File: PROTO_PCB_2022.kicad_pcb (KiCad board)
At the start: 2 copper layers, 0 parts

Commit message: Updated ECU connector
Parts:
- added BRAKELIGHTS_EN1: Conn_?, Footprint Library:Molex_Proto_Microfit_Footprint, F.Cu at (193.0, 104.1)
- added BRAKELIGHTS_MOSFET1: Q3, Package_TO_SOT_SMD:SOT-23, F.Cu at (164.8, 123.2)
- added HORN_EN1: Conn_?, Footprint Library:Molex_Proto_Microfit_Footprint, F.Cu at (193.0, 129.5)
- added HORN_MOSFET1: Q1, Package_TO_SOT_SMD:SOT-23, F.Cu at (165.1, 130.8)
- added J1: ECU_EN_CONNECTION, Connector_Molex:Molex_CLIK-Mate_502386-0470_1x04-1MP_P1.25mm_Horizontal, F.Cu at (115.6, 96.5)
- added J2: SMALL_12V_BATTERY_CONNECTOR, TerminalBlock_Phoenix:TerminalBlock_Phoenix_PT-1,5-2-5.0-H_1x02_P5.00mm_Horizontal, F.Cu at (113.0, 124.5)
- added J3: 12V_EXTRA, TerminalBlock_Phoenix:TerminalBlock_Phoenix_PT-1,5-2-5.0-H_1x02_P5.00mm_Horizontal, F.Cu at (113.0, 152.4)
- added K1: RT214012, Relay_THT:Relay_SPDT_Schrack-RT1-FormC_RM5mm, F.Cu at (141.0, 108.0)
- added K2: RT214012, Relay_THT:Relay_SPDT_Schrack-RT1-FormC_RM5mm, F.Cu at (141.0, 156.2)
- added R1: 10k, Resistor_SMD:R_0805_2012Metric, F.Cu at (153.7, 129.5)
- added R2: 10k, Resistor_SMD:R_0805_2012Metric, F.Cu at (153.7, 121.9)
- added STARTER_MOTOR_EN1: Conn_?, Footprint Library:Molex_Proto_Microfit_Footprint, F.Cu at (193.0, 154.9)

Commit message: added new TVS diodes to schematic
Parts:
- added D1: HORN_D_TVS, Diode_SMD:D_SMB, F.Cu at (214.6, 92.7)
- added D2: BRAKELIGHTS_D_TVS, Diode_SMD:D_SMB, F.Cu at (209.6, 82.5)
- added J1: ECU_EN_CONNECTON_1, Connector_Molex:Molex_Micro-Fit_3.0_43650-0215_1x02_P3.00mm_Vertical, F.Cu at (166.3, 65.3)
- added J4: ECU_EN_CONECTION_2, Connector_Molex:Molex_Micro-Fit_3.0_43650-0215_1x02_P3.00mm_Vertical, F.Cu at (196.8, 71.1)
- added J5: ECU_EN_CONECTION_3, Connector_Molex:Molex_Micro-Fit_3.0_43650-0215_1x02_P3.00mm_Vertical, F.Cu at (178.0, 65.3)
- Q1: renamed from HORN_MOSFET1; value Q1 -> HORN_MOSFET1
- Q2: renamed from BRAKELIGHTS_MOSFET1; value Q3 -> BRAKELIGHTS_MOSFET1
- moved J3 41.3 mm to (85.1, 121.9)
- moved J2 41.3 mm to (85.1, 94.0)
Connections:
- J2 pad 2: SMALL_12V -> ECU_KILL_EN_TOGGLESWITCH_1A
- J3 pad 2: SMALL_12V -> ECU_KILL_EN_TOGGLESWITCH_1A
- K2 pad 14: SMALL_12V -> ECU_KILL_EN_TOGGLESWITCH_1A
- Q1 pad 1: SMALL_12V -> ECU_KILL_EN_TOGGLESWITCH_1A
- Q2 pad 1: SMALL_12V -> ECU_KILL_EN_TOGGLESWITCH_1A

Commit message: board layout done
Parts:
- removed the J1 at (115.6, 96.5)
- removed K1: RT214012, Relay_THT:Relay_SPDT_Schrack-RT1-FormC_RM5mm
- moved STARTER_MOTOR_EN1 118.1 mm to (97.8, 85.1), turned to 90 degrees
- moved J3 86.9 mm to (163.8, 85.1), turned to 180 degrees
- moved D1 82.9 mm to (134.6, 114.3)
- moved J4 77.3 mm to (120.7, 83.8)
- moved K2 76.8 mm to (92.7, 96.5), turned to 270 degrees
- moved D2 76.5 mm to (134.6, 97.8)
- moved J5 72.4 mm to (108.0, 83.8)
- moved J2 66.6 mm to (151.1, 85.1), turned to 180 degrees
- moved Q2 37.9 mm to (132.1, 104.1), turned to 270 degrees
- moved J1 37.8 mm to (133.3, 83.8)
- moved Q1 34.2 mm to (132.1, 121.9), turned to 270 degrees
- moved HORN_EN1 29.9 mm to (163.8, 123.2)
- moved BRAKELIGHTS_EN1 29.2 mm to (163.8, 105.4)
- moved R2 24.3 mm to (137.2, 104.1), turned to 270 degrees
- moved R1 18.2 mm to (137.2, 121.9), turned to 270 degrees

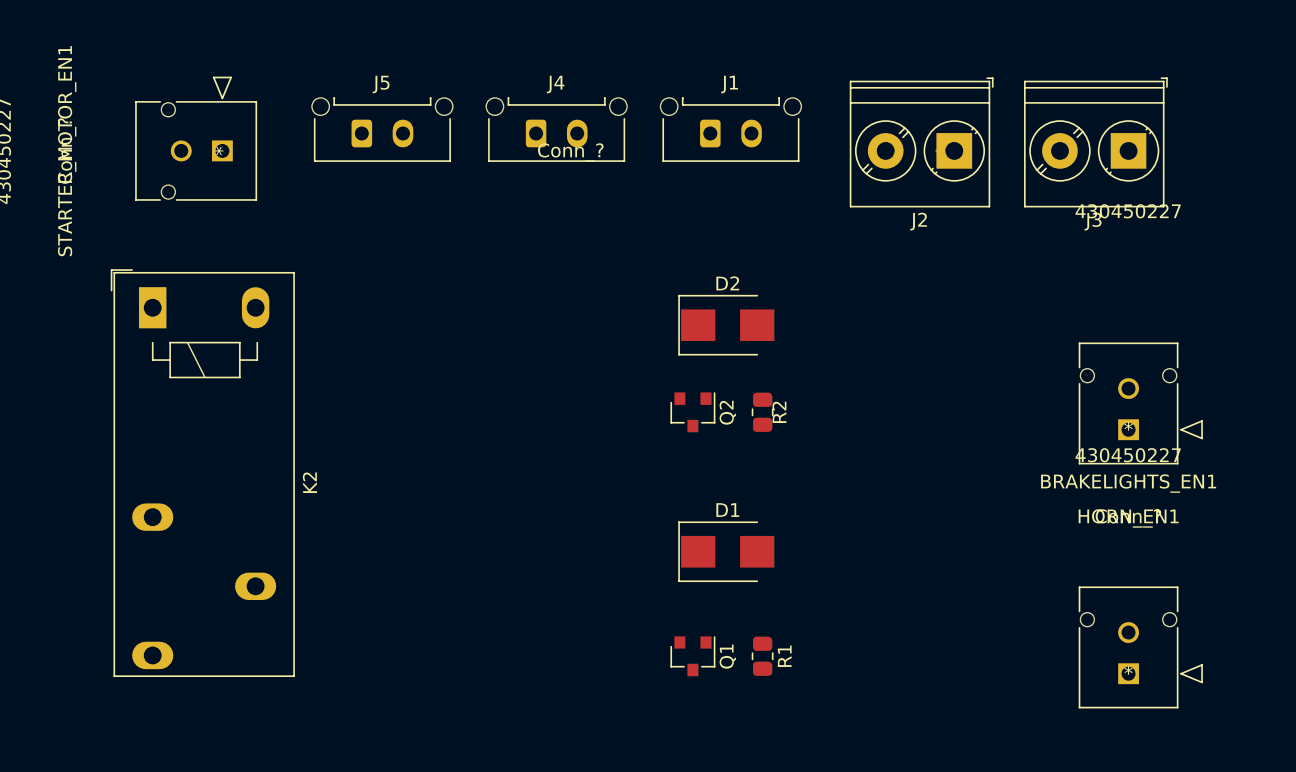
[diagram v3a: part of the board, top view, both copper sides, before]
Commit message: layout completed: components arranged, traces created
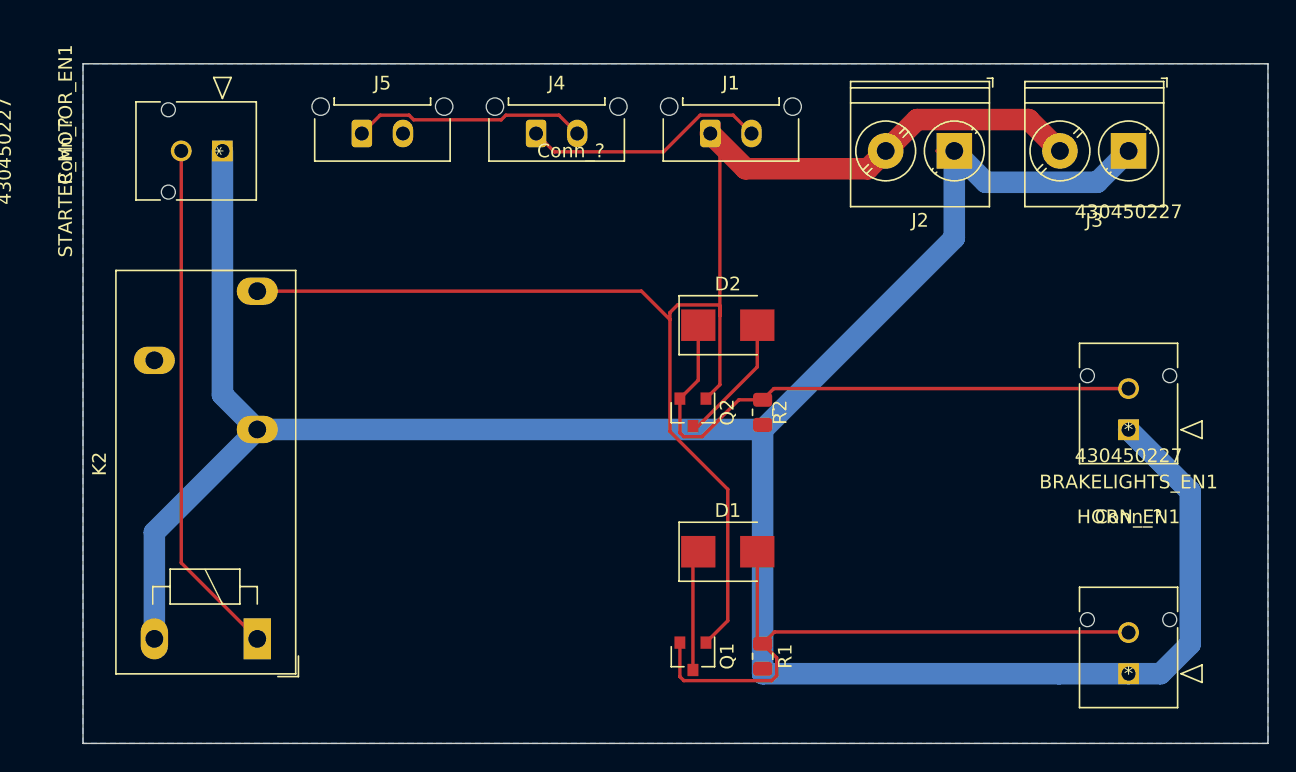
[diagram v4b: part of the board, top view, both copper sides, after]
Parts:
- moved K2 25.3 mm to (100.3, 120.7), turned to 90 degrees
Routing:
- net GND: track 0.08 -> 184.7 mm
- net ECU_KILL_EN_TOGGLESWITCH_1A: track 0.00 -> 111.0 mm
- net HORN_EN_12V_SIGNAL: track 0.00 -> 46.5 mm
- net BRAKELIGHTS_EN_12V_SIGNAL: track 0.00 -> 42.7 mm
- net STARTER_EN_PUSHBUTTON: track 0.00 -> 37.9 mm
- net ECU_KILL_EN_TOGGLESWITCH_1B: track 0.00 -> 17.9 mm
- net ECU_KILL_EN_TOGGLESWITCH_2B: track 0.00 -> 17.1 mm
- net BRAKELIGHTS_PWR: track 0.00 -> 9.52 mm
- net HORN_PWR: track 0.00 -> 8.78 mm
- added copper zone on B.Cu, net GND
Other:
- board outline added: 86.4 x 49.5 mm

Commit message: Draft PCB for Report Purposes
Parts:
- removed the J1 at (133.3, 83.8)
- removed the J4 at (120.7, 83.8)
- removed the J5 at (108.0, 83.8)
- added J10: VESC_EN_SIGNAL, Footprint Library:Molex_Proto_Microfit_Footprint, F.Cu at (112.4, 84.5)
- added J11: BRAKELIGHTS_PWR_OUT, Footprint Library:Molex_Proto_Microfit_Footprint, F.Cu at (80.2, 84.5)
- added J12: HORN_PWR_OUT, Footprint Library:Molex_Proto_Microfit_Footprint, F.Cu at (96.5, 84.5)
- added J6: ECU_POWER_DIST, TerminalBlock_Phoenix:TerminalBlock_Phoenix_PT-1,5-2-5.0-H_1x02_P5.00mm_Horizontal, F.Cu at (156.8, 111.8)
- added J7: ECU_KILL_1, Footprint Library:Molex_Proto_Microfit_Footprint, F.Cu at (128.3, 84.5)
- added J8: ECU_KILL_2, Footprint Library:Molex_Proto_Microfit_Footprint, F.Cu at (144.7, 84.5)
- added J9: ECU_KILL_3, Footprint Library:Molex_Proto_Microfit_Footprint, F.Cu at (161.1, 84.5)
- D1: renamed from D2; value BRAKELIGHTS_D_TVS -> (none)
- D2: renamed from D1; value HORN_D_TVS -> (none)
- J1: renamed from HORN_EN1; value Conn_? -> HORN_EN1
- J2: renamed from BRAKELIGHTS_EN1; value Conn_? -> BRAKELIGHTS_EN1
- J3: renamed from STARTER_MOTOR_EN1; value Conn_? -> STARTER_MOTOR_EN
- J4: renamed from J2; value SMALL_12V_BATTERY_CONNECTOR -> 12V_BATT1
- K1: renamed from K2; value RT214012 -> (none)
- Q1: renamed from Q2; value BRAKELIGHTS_MOSFET1 -> (none)
- Q2: renamed from Q1; value HORN_MOSFET1 -> (none)
- R1: renamed from R2; value 10k -> (none)
- R2: renamed from R1; value 10k -> (none)
- moved J2 87.7 mm to (76.4, 112.4), turned to 270 degrees
- moved J1 71.9 mm to (92.8, 112.4), turned to 270 degrees
- moved D1 59.1 mm to (75.6, 98.8), turned to 90 degrees
- moved R1 55.7 mm to (81.6, 101.6), turned to 0 degrees
- moved K1 54.3 mm to (148.0, 94.6), turned to 180 degrees
- moved Q1 51.0 mm to (81.5, 96.9), turned to 0 degrees
- moved D2 45.3 mm to (92.1, 98.7), turned to 270 degrees
- moved R2 44.1 mm to (98.1, 101.5), turned to 0 degrees
- moved Q2 42.3 mm to (98.1, 96.9), turned to 0 degrees
- moved J4 37.7 mm to (124.5, 111.8), turned to 0 degrees
- moved J5 35.3 mm to (140.7, 111.8), turned to 0 degrees
- moved J3 29.4 mm to (108.6, 112.4), turned to 270 degrees
- renumbered J3 to J5
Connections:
- D1 pad 2: BRAKELIGHTS_PWR -> GND
- D2 pad 1: HORN_PWR -> GND
- K1 pad 11: VESC_POWER_CONNECTION -> VESC_EN_SIGNAL
- Q1 pad 1: ECU_KILL_EN_TOGGLESWITCH_1A -> BRAKELIGHTS_PWR_OUT
- Q1 pad 3: BRAKELIGHTS_PWR -> GND
- Q2 pad 1: ECU_KILL_EN_TOGGLESWITCH_1A -> HORN_PWR_OUT
- Q2 pad 3: HORN_PWR -> GND
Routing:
- net GND: track 184.7 -> 26.5 mm, vias 0 -> 10
- net ECU_KILL_EN_TOGGLESWITCH_1A: track 111.0 -> 60.9 mm
- net ECU_KILL_EN_TOGGLESWITCH_3B: track 0.00 -> 27.6 mm
- net VESC_EN_SIGNAL: track 0.00 -> 26.2 mm
- net STARTER_EN_PUSHBUTTON: track 37.9 -> 63.4 mm
- net HORN_EN_12V_SIGNAL: track 46.5 -> 23.4 mm
- net BRAKELIGHTS_EN_12V_SIGNAL: track 42.7 -> 19.8 mm
- net HORN_PWR_OUT: track 0.00 -> 12.9 mm
- net BRAKELIGHTS_PWR_OUT: track 0.00 -> 12.9 mm
- net BRAKELIGHTS_PWR: track 9.52 -> 0.00 mm
- net HORN_PWR: track 8.78 -> 0.00 mm
- net ECU_KILL_EN_TOGGLESWITCH_1B: track 17.9 -> 13.5 mm
- net ECU_KILL_EN_TOGGLESWITCH_2B: track 17.1 -> 13.4 mm
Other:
- board size 86.4 x 49.5 mm -> 94 x 39.4 mm
- board text added: "UBC Supermileage Proto SAE 2022"

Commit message: second version
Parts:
- removed the J11 at (80.2, 84.5)
- removed the J12 at (96.5, 84.5)
- removed K1: , Relay_THT:Relay_SPDT_Schrack-RT1-FormC_RM5mm
- added H1: MountingHole, MountingHole:MountingHole_2.7mm_M2.5, F.Cu at (155.6, 98.4)
- added H2: MountingHole, MountingHole:MountingHole_2.7mm_M2.5, F.Cu at (77.5, 98.4)
- added J3: BRAKELIGHTS_CONN, TerminalBlock_Phoenix:TerminalBlock_Phoenix_PT-1,5-2-5.0-H_1x02_P5.00mm_Horizontal, F.Cu at (80.6, 85.1)
- added J6: HORN_CONN, TerminalBlock_Phoenix:TerminalBlock_Phoenix_PT-1,5-2-5.0-H_1x02_P5.00mm_Horizontal, F.Cu at (92.7, 85.1)
- added R3: , Resistor_SMD:R_0603_1608Metric, F.Cu at (110.2, 91.9)
- added U1: , Package_TO_SOT_SMD:SOT-223-3_TabPin2, F.Cu at (120.4, 98.6)
- R1: renamed from R2; value (none) -> 10k
- moved D1 12.8 mm to (104.9, 98.9)
- moved D2 11.4 mm to (87.0, 98.8)
- moved Q2 11.4 mm to (93.0, 96.9)
- moved R2 11.4 mm to (93.0, 101.6)
- moved J10 4.45 mm to (140.3, 84.5)
- moved J11 4.45 mm to (156.7, 84.5)
- moved J9 4.45 mm to (123.8, 84.5)
- moved J5 4.44 mm to (108.0, 84.5)
- moved J8 4.44 mm to (152.4, 111.8)
- moved J7 3.17 mm to (127.7, 111.8)
- moved J1 2.54 mm to (95.3, 112.4)
- moved J2 2.54 mm to (79.0, 112.4)
- moved J4 2.54 mm to (111.1, 112.4)
- moved R1 0.65 mm to (98.7, 101.6)
- moved Q1 0.64 mm to (98.7, 96.9)
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- renumbered D2 to D1, D1 to D2, J8 to J10, J9 to J11, J5 to J12, J3 to J4, J10 to J5, J4 to J7, J6 to J8, J7 to J9, Q2 to Q1, Q1 to Q2, R1 to R2
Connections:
- net ECU_KILL_EN_TOGGLESWITCH_1A renamed 12V_FOR_BRAKELIGHTS
- D1 pad 2: HORN_EN_12V_SIGNAL -> HORN_EN_5V
- D2 pad 1: BRAKELIGHTS_EN_12V_SIGNAL -> BRAKELIGHTS_EN_5V
- J1 pad 1: GND -> HORN_EN_5V
- J1 pad 2: HORN_EN_12V_SIGNAL -> +5V
- J2 pad 1: GND -> BRAKELIGHTS_EN_5V
- J2 pad 2: BRAKELIGHTS_EN_12V_SIGNAL -> +5V
- J4 pad 1: GND -> VESC_EN_5V
- J4 pad 2: STARTER_EN_PUSHBUTTON -> +5V
- J5 pad 1: GND -> Net-(J5-Pad1)
- J5 pad 2: VESC_EN_SIGNAL -> VESC_EN_5V
- Q1 pad 1: HORN_PWR_OUT -> HORN_GND
- Q1 pad 2: HORN_EN_12V_SIGNAL -> HORN_EN_5V
- Q2 pad 1: BRAKELIGHTS_PWR_OUT -> BRAKELIGHTS_GND
- Q2 pad 2: BRAKELIGHTS_EN_12V_SIGNAL -> BRAKELIGHTS_EN_5V
- R1 pad 1: HORN_EN_12V_SIGNAL -> HORN_EN_5V
- R2 pad 1: BRAKELIGHTS_EN_12V_SIGNAL -> BRAKELIGHTS_EN_5V
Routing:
- net STARTER_EN_PUSHBUTTON: track 63.4 -> 0.00 mm
- net +5V: track 0.00 -> 61.1 mm
- net 12V_FOR_BRAKELIGHTS: track 60.9 -> 98.3 mm
- net VESC_EN_5V: track 0.00 -> 30.5 mm
- net VESC_EN_SIGNAL: track 26.2 -> 0.00 mm
- net HORN_EN_5V: track 0.00 -> 24.8 mm
- net BRAKELIGHTS_EN_5V: track 0.00 -> 24.6 mm
- net HORN_EN_12V_SIGNAL: track 23.4 -> 0.00 mm
- net BRAKELIGHTS_EN_12V_SIGNAL: track 19.8 -> 0.00 mm
- net BRAKELIGHTS_GND: track 0.00 -> 15.8 mm
- net HORN_GND: track 0.00 -> 12.9 mm
- net HORN_PWR_OUT: track 12.9 -> 0.00 mm
- net BRAKELIGHTS_PWR_OUT: track 12.9 -> 0.00 mm
- net Net-(J5-Pad1): track 0.00 -> 8.78 mm
- net ECU_KILL_EN_TOGGLESWITCH_3B: track 27.6 -> 31.2 mm
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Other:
- board size 94 x 39.4 mm -> 92.1 x 40.6 mm

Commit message: second version
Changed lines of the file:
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@@
   (layers
     (0 F.Cu signal)
-    (31 B.Cu signal hide)
+    (31 B.Cu signal)
     (32 B.Adhes user)
     (33 F.Adhes user)
@@
   )
   (setup
-    (last_trace_width 1.57)
+    (last_trace_width 2.5)
     (user_trace_width 1.57)
+    (user_trace_width 2.5)
     (user_trace_width 3.14)
     (trace_clearance 0.2)
@@
   (module "Footprint Library:Molex_Proto_Microfit_Footprint" (layer F.Cu)
     (at 123.825 84.455 90)
-    (fp_text reference J9 (at -6.477 -2.413 180) (layer F.SilkS)
-      (effects (font (size 1 1) (thickness 0.15)))
-    )
+    (fp_text reference J9 (at -6.477 -1.905 180) (layer F.SilkS)
+      (effects (font (size 1 1) (thickness 0.15)))
+    )

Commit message: almost final version
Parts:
- removed the J11 at (156.7, 84.5)
- added C1: 1u, Capacitor_SMD:C_1206_3216Metric, F.Cu at (127.0, 98.6)
- added C2: 4.7u, Capacitor_SMD:C_1206_3216Metric, F.Cu at (112.8, 98.6)
- added F1: Fuse, Fuse:Fuseholder_Blade_ATO_Littelfuse_Pudenz_2_Pin, F.Cu at (136.1, 100.8)
- added J8: ECU_1, TerminalBlock_Phoenix:TerminalBlock_Phoenix_PT-1,5-2-5.0-H_1x02_P5.00mm_Horizontal, F.Cu at (104.4, 85.1)
- added R1: 4.7k, Resistor_SMD:R_1206_3216Metric, F.Cu at (82.8, 100.1)
- added R4: 4.7k, Resistor_SMD:R_1206_3216Metric, F.Cu at (82.8, 95.0)
- added TP1: TestPoint, TestPoint:TestPoint_Keystone_5015_Micro-Minature, F.Cu at (134.1, 94.2)
- added TP2: TestPoint, TestPoint:TestPoint_Keystone_5015_Micro-Minature, F.Cu at (112.8, 95.0)
- added TP3: TestPoint, TestPoint:TestPoint_Keystone_5015_Micro-Minature, F.Cu at (104.6, 95.0)
- D1, D2: value (none) -> LED; footprint Diode_SMD:D_SMB -> Resistor_SMD:R_0603_1608Metric
- J1: footprint Footprint Library:Molex_Proto_Microfit_Footprint -> footprints:436500201
- J10: value ECU_KILL_2 -> ECU_3; footprint Footprint Library:Molex_Proto_Microfit_Footprint -> TerminalBlock_Phoenix:TerminalBlock_Phoenix_PT-1,5-2-5.0-H_1x02_P5.00mm_Horizontal
- J11: renamed from J7; value 12V_BATT1 -> 12V_IN
- J12: value 12V_EXTRA -> 12V_OUT_EXTRA
- J3: renamed from J4; footprint Footprint Library:Molex_Proto_Microfit_Footprint -> footprints:436500201
- J4: renamed from J5; footprint Footprint Library:Molex_Proto_Microfit_Footprint -> footprints:436500201
- J6: renamed from J2; footprint Footprint Library:Molex_Proto_Microfit_Footprint -> footprints:436500201
- J9: value ECU_KILL_1 -> ECU_2; footprint Footprint Library:Molex_Proto_Microfit_Footprint -> TerminalBlock_Phoenix:TerminalBlock_Phoenix_PT-1,5-2-5.0-H_1x02_P5.00mm_Horizontal
- Q1: value (none) -> HORN_MOSFET1
- Q2: value (none) -> BRAKELIGHTS_MOSFET1
- R2: renamed from R1; footprint Resistor_SMD:R_0805_2012Metric -> Resistor_SMD:R_1206_3216Metric
- R3: value (none) -> 10k; footprint Resistor_SMD:R_0603_1608Metric -> Resistor_SMD:R_1206_3216Metric
- R5: renamed from R2; value (none) -> 10k; footprint Resistor_SMD:R_0805_2012Metric -> Resistor_SMD:R_1206_3216Metric
- U1: value (none) -> LD1117S50TR_SOT223
- moved J4 31.1 mm to (121.9, 112.3), turned to 270 degrees
- moved J5 29.1 mm to (140.7, 85.1), turned to 180 degrees
- moved D1 18.1 mm to (86.9, 99.9)
- moved J10 11.7 mm to (128.6, 85.1), turned to 180 degrees
- moved R3 11.0 mm to (104.6, 101.3), turned to 90 degrees
- moved H1 8.58 mm to (147.8, 94.7)
- moved J9 7.37 mm to (116.5, 85.1), turned to 180 degrees
- moved D2 3.82 mm to (86.9, 95.0), turned to 270 degrees
- moved J6 3.35 mm to (82.3, 112.4)
- moved H2 2.45 mm to (75.2, 99.3)
- moved J3 2.40 mm to (108.7, 112.3)
- moved Q1 1.83 mm to (97.7, 95.4)
- moved R2 1.83 mm to (97.7, 100.1)
- moved R5 1.83 mm to (92.0, 100.1)
- moved Q2 1.75 mm to (91.9, 95.5)
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- renumbered J6 to J2, J8 to J5, J3 to J7
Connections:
- D1 pad 1: GND -> Net-(D1-Pad1)
- D2 pad 1: BRAKELIGHTS_EN_5V -> Net-(D2-Pad1)
- D2 pad 2: GND -> BRAKELIGHTS_EN_5V
- J10 pad 1: ECU_KILL_EN_TOGGLESWITCH_2B -> ECU_KILL_EN_TOGGLESWITCH_3B
- J10 pad 2: ECU_KILL_EN_TOGGLESWITCH_1B -> ECU_KILL_EN_TOGGLESWITCH_2B
- J11 pad 2: 12V_FOR_BRAKELIGHTS -> BATT_12V
- J4 pad 1: Net-(J5-Pad1) -> GND
- J9 pad 1: ECU_KILL_EN_TOGGLESWITCH_1B -> ECU_KILL_EN_TOGGLESWITCH_2B
- J9 pad 2: 12V_FOR_BRAKELIGHTS -> ECU_KILL_EN_TOGGLESWITCH_1B
- R3 pad 1: Net-(J5-Pad1) -> VESC_EN_5V
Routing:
- net 12V_FOR_BRAKELIGHTS: track 98.3 -> 68.5 mm
- net ECU_KILL_EN_TOGGLESWITCH_3B: track 31.2 -> 7.12 mm
- net Net-(J5-Pad1): track 8.78 -> 0.00 mm
- net GND: track 28.6 -> 21.3 mm, vias 8 -> 27
- net HORN_EN_5V: track 24.8 -> 31.6 mm
- net BRAKELIGHTS_EN_5V: track 24.6 -> 31.3 mm, vias 0 -> 4
- net ECU_KILL_EN_TOGGLESWITCH_1B: track 13.5 -> 7.12 mm
- net ECU_KILL_EN_TOGGLESWITCH_2B: track 13.4 -> 7.12 mm
- net +5V: track 61.1 -> 66.4 mm
- net Net-(D2-Pad1): track 0.00 -> 4.33 mm
- net Net-(D1-Pad1): track 0.00 -> 4.25 mm
- net HORN_GND: track 12.9 -> 10.3 mm
- net VESC_EN_5V: track 30.5 -> 28.3 mm, vias 0 -> 4
- net BRAKELIGHTS_GND: track 15.8 -> 15.2 mm
- added copper zone on F.Cu, net +5V
- added copper zone on F.Cu, net 12V_FOR_BRAKELIGHTS
- added copper zone on F.Cu, net BATT_12V
- added copper zone on F.Cu, net GND
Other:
- board size 92.1 x 40.6 mm -> 81.4 x 40.6 mm
- board text added: "12V"
- board text added: "5V"
- board text added: "GND"
- board text added: "HORN"
- board text added: "LIGHTS"
- board text added: "“Steak&Shake” Main PCB"
